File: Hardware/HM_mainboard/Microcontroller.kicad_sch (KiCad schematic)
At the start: 13 parts, among them J2 USB_C_Receptacle_USB2.0, U3 ESP32-S3-WROOM-1, Y1 32.768 kHz

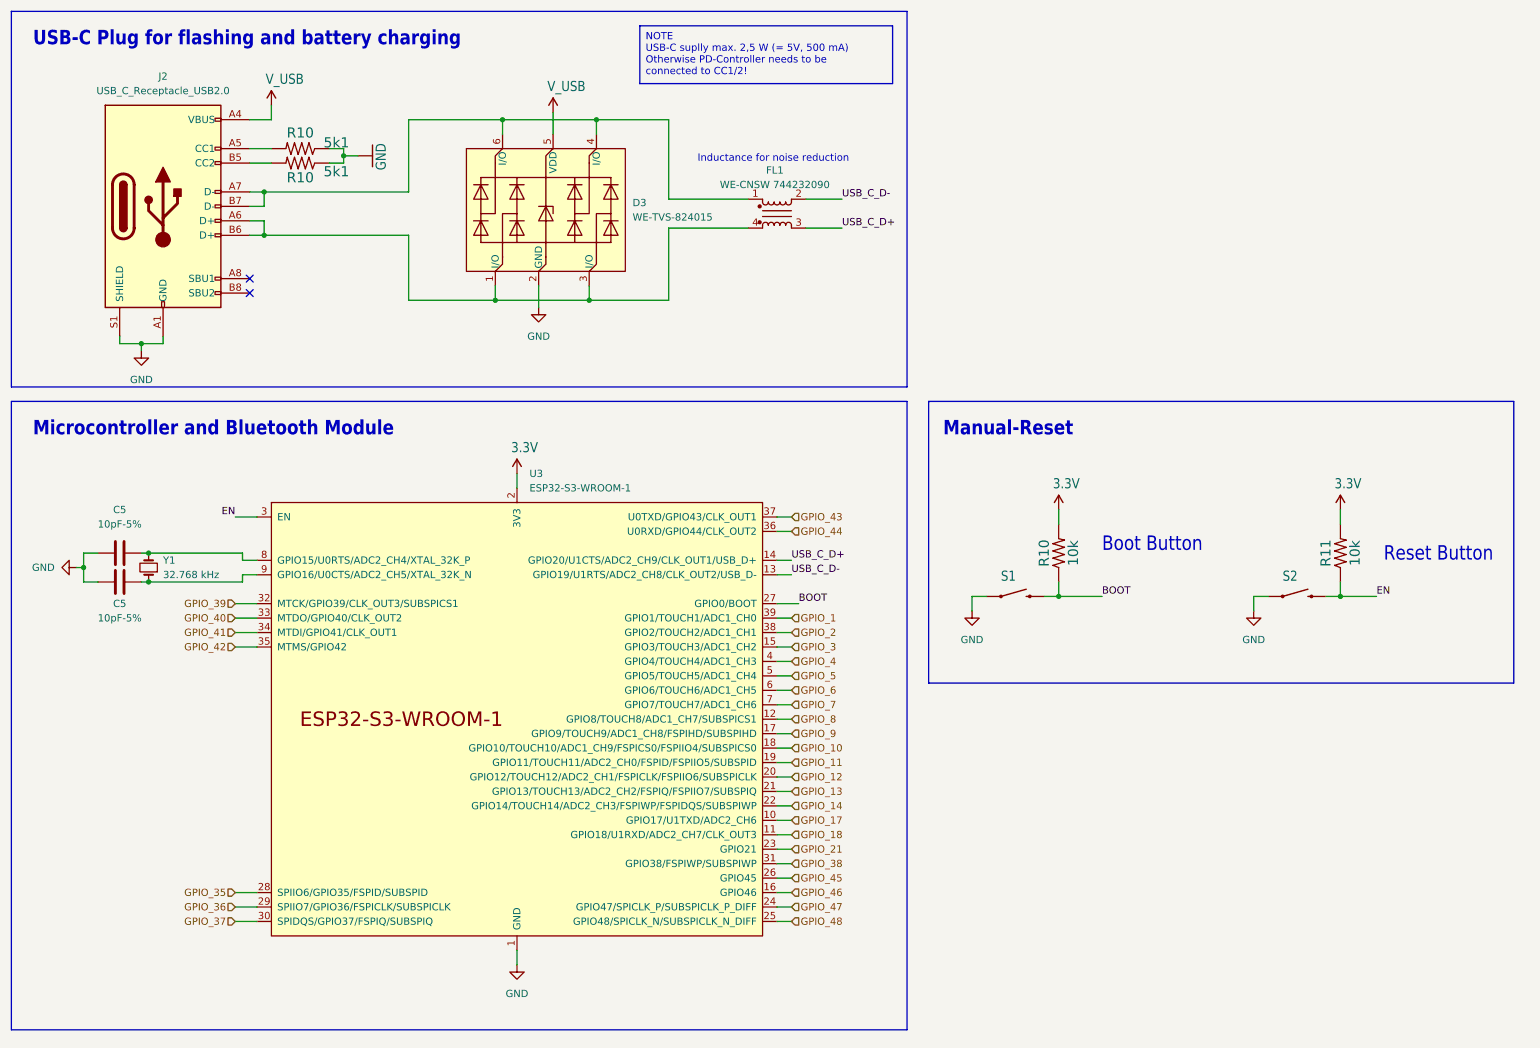
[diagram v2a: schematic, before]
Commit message: Added IMUs, updated some components
- Added 2 additonal IMUs:
     1) 6-Axis MC6470
     2) 9-Axis BNO55
- Replaced button jack connectors
- Replaced battery charging LED by a charging status measurement circuit
- Replaced caps for clock crystal
- Added stabalizing caps to uC Vcc
- Added UART pin header
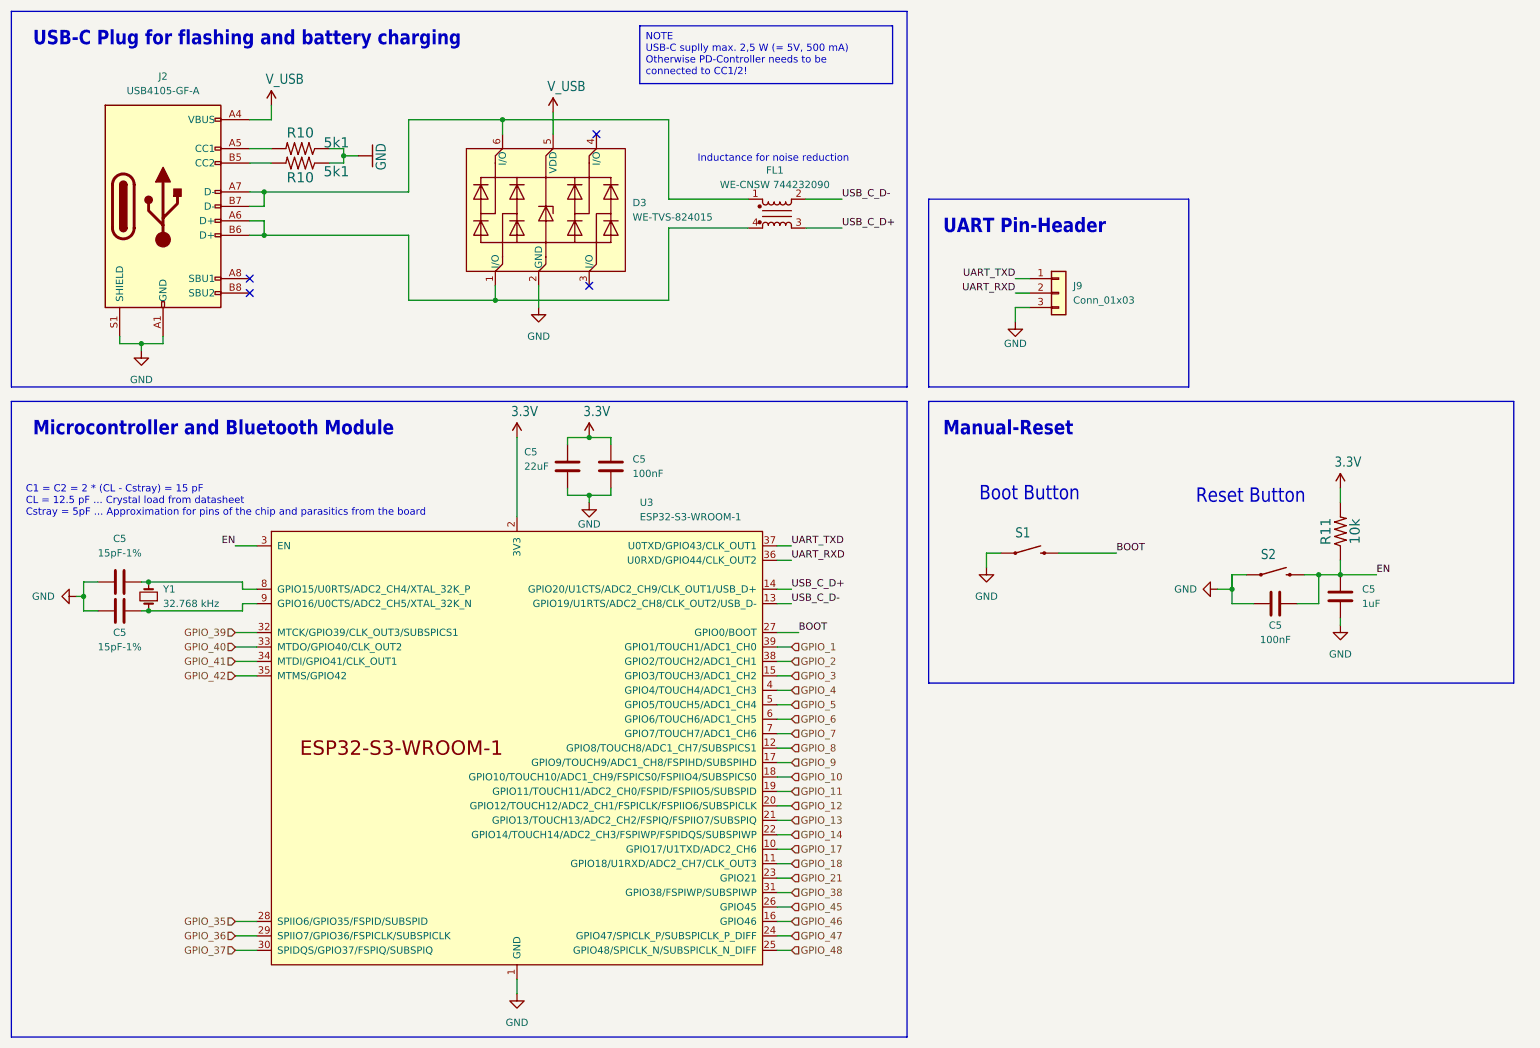
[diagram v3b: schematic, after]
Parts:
- removed R10: 10k, Resistor_SMD:R_0603_1608Metric_Pad0.98x0.95mm_HandSolder, symbol esp32-thing-eagle-import:10KOHM-1/10W-1%(0603)0603
- added C5 (x2): 100nF, Capacitor_SMD:C_0603_1608Metric_Pad1.08x0.95mm_HandSolder, symbol Device:C
- added C5: 22uF, Capacitor_SMD:C_0603_1608Metric_Pad1.08x0.95mm_HandSolder, symbol Device:C
- added C5: 1uF, Capacitor_SMD:C_0603_1608Metric_Pad1.08x0.95mm_HandSolder, symbol Device:C
- added J9: Conn_01x03, Connector_PinHeader_2.54mm:PinHeader_1x03_P2.54mm_Vertical, symbol Connector_Generic:Conn_01x03
- C5: value 10pF-5% -> 15pF-1%; footprint Capacitor_SMD:C_0201_0603Metric_Pad0.64x0.40mm_HandSolder -> Capacitor_SMD:C_0603_1608Metric_Pad1.08x0.95mm_HandSolder; Mouser (none) -> C0603C150F8HACAUTO
- J2: value USB_C_Receptacle_USB2.0 -> USB4105-GF-A; footprint (none) -> Connector_USB:USB_C_Receptacle_GCT_USB4105-xx-A_16P_TopMnt_Horizontal
- R10: footprint Resistor_SMD:R_0201_0603Metric_Pad0.64x0.40mm_HandSolder -> Resistor_SMD:R_0603_1608Metric_Pad0.98x0.95mm_HandSolder
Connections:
- net 3.3V: now also C5.2, C5.2
- net EN: now also C5.2, C5.2
- net GND: now also C5.1, C5.1, C5.1, C5.1, J9.3 (Pin_3)
- net at D3.1 (I/O), FL1.4, J2.A6 (D+)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: no longer D3.3 (I/O)
- net at D3.6 (I/O), FL1.1, J2.A7 (D-)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: no longer D3.4 (I/O)
- net GPIO_43 renamed UART_TXD
- net UART_TXD: now also J9.1 (Pin_1)
- net GPIO_44 renamed UART_RXD
- net UART_RXD: now also J9.2 (Pin_2)
- no-connect marks 2 -> 4
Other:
- note added: "C1 = C2 = 2 * (CL - Cstray) = 15 pF CL = 12.5 pF ... Crystal load from datasheet Cstray = 5pF ... Approximation for pins of the chip and parasitics from the board"
- note added: "UART Pin-Header"
- moved on the sheet: C5, R11, S1, S2, U3, Y1

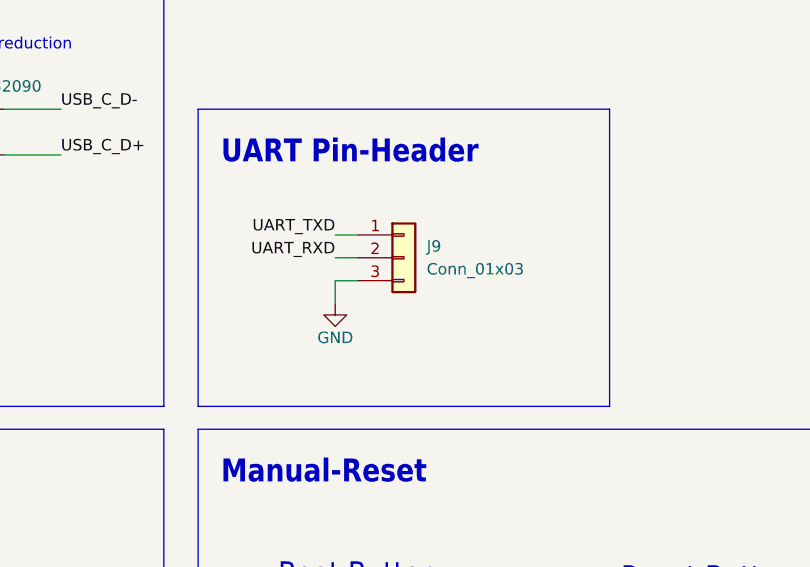
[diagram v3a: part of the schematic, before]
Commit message: Changed I2C address selection of IMUs
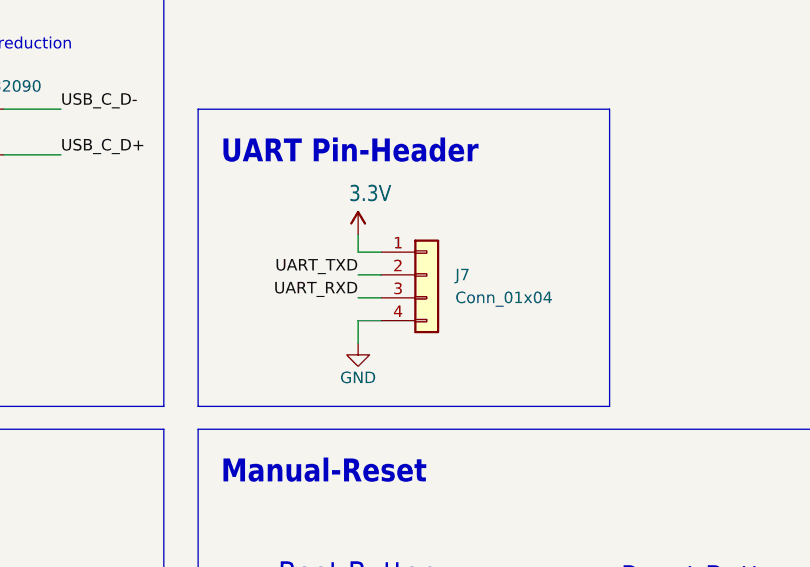
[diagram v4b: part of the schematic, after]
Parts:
- removed J9: Conn_01x03, Connector_PinHeader_2.54mm:PinHeader_1x03_P2.54mm_Vertical, symbol Connector_Generic:Conn_01x03
- added J7: Conn_01x04, symbol Connector_Generic:Conn_01x04
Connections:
- net 3.3V: now also J7.1 (Pin_1)
- net GND: now also J7.4 (Pin_4)
- net UART_RXD: now also J7.3 (Pin_3)
- net UART_TXD: now also J7.2 (Pin_2)
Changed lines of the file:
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@@
+    (stroke (width 0) (type default))
+  )
+  (wire (pts (xy 195.58 62.23) (xy 195.58 64.135))
     (stroke (width 0) (type default))
   )
@@
     (stroke (width 0) (type default))
   )
-  (wire (pts (xy 193.04 62.23) (xy 195.58 62.23))
+  (wire (pts (xy 195.58 64.135) (xy 198.12 64.135))
+    (stroke (width 0) (type default))
+  )
+  (wire (pts (xy 195.58 66.675) (xy 198.12 66.675))
     (stroke (width 0) (type default))
   )
@@
     (stroke (width 0) (type default))
   )
-  (wire (pts (xy 193.04 67.31) (xy 195.58 67.31))
-    (stroke (width 0) (type default))
-  )
-  (wire (pts (xy 193.04 69.85) (xy 193.04 67.31))
+  (wire (pts (xy 195.58 71.755) (xy 198.12 71.755))
+    (stroke (width 0) (type default))
+  )
+  (wire (pts (xy 195.58 74.295) (xy 195.58 71.755))
     (stroke (width 0) (type default))
   )
@@
     (stroke (width 0) (type default))
   )
-  (wire (pts (xy 193.04 64.77) (xy 195.58 64.77))
+  (wire (pts (xy 195.58 69.215) (xy 198.12 69.215))
     (stroke (width 0) (type default))
   )
@@
     (effects (font (size 1.27 1.27)) (justify left bottom))
   )
-  (label "UART_RXD" (at 193.04 64.77 180) (fields_autoplaced)
+  (label "UART_RXD" (at 195.58 69.215 180) (fields_autoplaced)
     (effects (font (size 1.27 1.27)) (justify right bottom))
   )
@@
     (effects (font (size 1.27 1.27)) (justify left bottom))
   )
-  (label "UART_TXD" (at 193.04 62.23 180) (fields_autoplaced)
+  (label "UART_TXD" (at 195.58 66.675 180) (fields_autoplaced)
     (effects (font (size 1.27 1.27)) (justify right bottom))
   )
@@
     )
   )
-  (symbol (lib_name "GND_1") (lib_id "power:GND") (at 193.04 69.85 0) (unit 1)
-    (in_bom yes) (on_board yes) (dnp no)
-    (property "Reference" "#PWR06" (at 193.04 76.2 0)
-      (effects (font (size 1.27 1.27)) hide)
-    )
-    (property "Value" "GND" (at 193.04 73.66 0)
-      (effects (font (size 1.27 1.27)))
-    )
-    (property "Footprint" "" (at 193.04 69.85 0)
-      (effects (font (size 1.27 1.27)) hide)
-    )
-    (property "Datasheet" "" (at 193.04 69.85 0)
+  (symbol (lib_name "GND_1") (lib_id "power:GND") (at 195.58 74.295 0) (unit 1)
+    (in_bom yes) (on_board yes) (dnp no)
+    (property "Reference" "#PWR06" (at 195.58 80.645 0)
+      (effects (font (size 1.27 1.27)) hide)
+    )
+    (property "Value" "GND" (at 195.58 78.105 0)
+      (effects (font (size 1.27 1.27)))
+    )
+    (property "Footprint" "" (at 195.58 74.295 0)
+      (effects (font (size 1.27 1.27)) hide)
+    )
+    (property "Datasheet" "" (at 195.58 74.295 0)
       (effects (font (size 1.27 1.27)) hide)
     )
@@
     )
   )
+  (symbol (lib_id "esp32-thing-eagle-import:3.3V") (at 195.58 62.23 0) (unit 1)
+    (in_bom yes) (on_board yes) (dnp no)
+    (property "Reference" "#SUPPLY08" (at 195.58 62.23 0)
+      (effects (font (size 1.27 1.27)) hide)
+    )
+    (property "Value" "3.3V" (at 194.564 58.674 0)
+      (effects (font (size 1.778 1.5113)) (justify left bottom))
+    )
+    (property "Footprint" "" (at 195.58 62.23 0)
+      (effects (font (size 1.27 1.27)) hide)
+    )
+    (property "Datasheet" "" (at 195.58 62.23 0)
+      (effects (font (size 1.27 1.27)) hide)
+    )
+    (pin "1")
+    (instances
+      (project "HM_mainboard"
+        (path "/54a6df43-5475-46a2-9916-8b0260700d4c"
+          (reference "#SUPPLY08") (unit 1)
+        )
+        (path "/54a6df43-5475-46a2-9916-8b0260700d4c/8a725ce3-408a-4762-9df2-b56094186e56"
+          (reference "#SUPPLY023") (unit 1)
+        )
+      )
+      (project "esp32-thing"
+        (path "/64c5aff3-bdec-4fb6-b5ec-87e5efa2adf7"
+          (reference "#SUPPLY8") (unit 1)
+        )
+      )
+    )
+  )
   (symbol (lib_id "Device:C") (at 35.56 120.65 90) (unit 1)
     (in_bom yes) (on_board yes) (dnp no)
@@
     )
   )
+  (symbol (lib_id "Connector_Generic:Conn_01x04") (at 203.2 66.675 0) (unit 1)
+    (in_bom yes) (on_board yes) (dnp no) (fields_autoplaced)
+    (property "Reference" "J7" (at 206.375 66.675 0)
+      (effects (font (size 1.27 1.27)) (justify left))
+    )
+    (property "Value" "Conn_01x04" (at 206.375 69.215 0)
+      (effects (font (size 1.27 1.27)) (justify left))
+    )
+    (property "Footprint" "" (at 203.2 66.675 0)
+      (effects (font (size 1.27 1.27)) hide)
+    )
+    (property "Datasheet" "~" (at 203.2 66.675 0)
+      (effects (font (size 1.27 1.27)) hide)
+    )
+    (pin "1")
+    (pin "2")
+    (pin "3")
+    (pin "4")
+    (instances
+      (project "HM_mainboard"
+        (path "/54a6df43-5475-46a2-9916-8b0260700d4c/8a725ce3-408a-4762-9df2-b56094186e56"
+          (reference "J7") (unit 1)
+        )
+      )
+    )
+  )
   (symbol (lib_name "GND_1") (lib_id "power:GND") (at 27.94 118.11 270) (unit 1)
     (in_bom yes) (on_board yes) (dnp no) (fields_autoplaced)
@@
         )
       )
-    )
-  )
-  (symbol (lib_id "Connector_Generic:Conn_01x03") (at 200.66 64.77 0) (unit 1)
-    (in_bom yes) (on_board yes) (dnp no) (fields_autoplaced)
-    (property "Reference" "J9" (at 203.2 63.5 0)
-      (effects (font (size 1.27 1.27)) (justify left))
-    )
-    (property "Value" "Conn_01x03" (at 203.2 66.04 0)
-      (effects (font (size 1.27 1.27)) (justify left))
-    )
-    (property "Footprint" "Connector_PinHeader_2.54mm:PinHeader_1x03_P2.54mm_Vertical" (at 200.66 64.77 0)
-      (effects (font (size 1.27 1.27)) hide)
-    )
-    (property "Datasheet" "~" (at 200.66 64.77 0)
-      (effects (font (size 1.27 1.27)) hide)
-    )
-    (pin "1")
-    (pin "2")
-    (pin "3")
-    (instances
-      (project "HM_mainboard"
-        (path "/54a6df43-5475-46a2-9916-8b0260700d4c/8a725ce3-408a-4762-9df2-b56094186e56"
-          (reference "J9") (unit 1)
-        )
-      )
